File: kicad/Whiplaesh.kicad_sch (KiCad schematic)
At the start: 0 parts

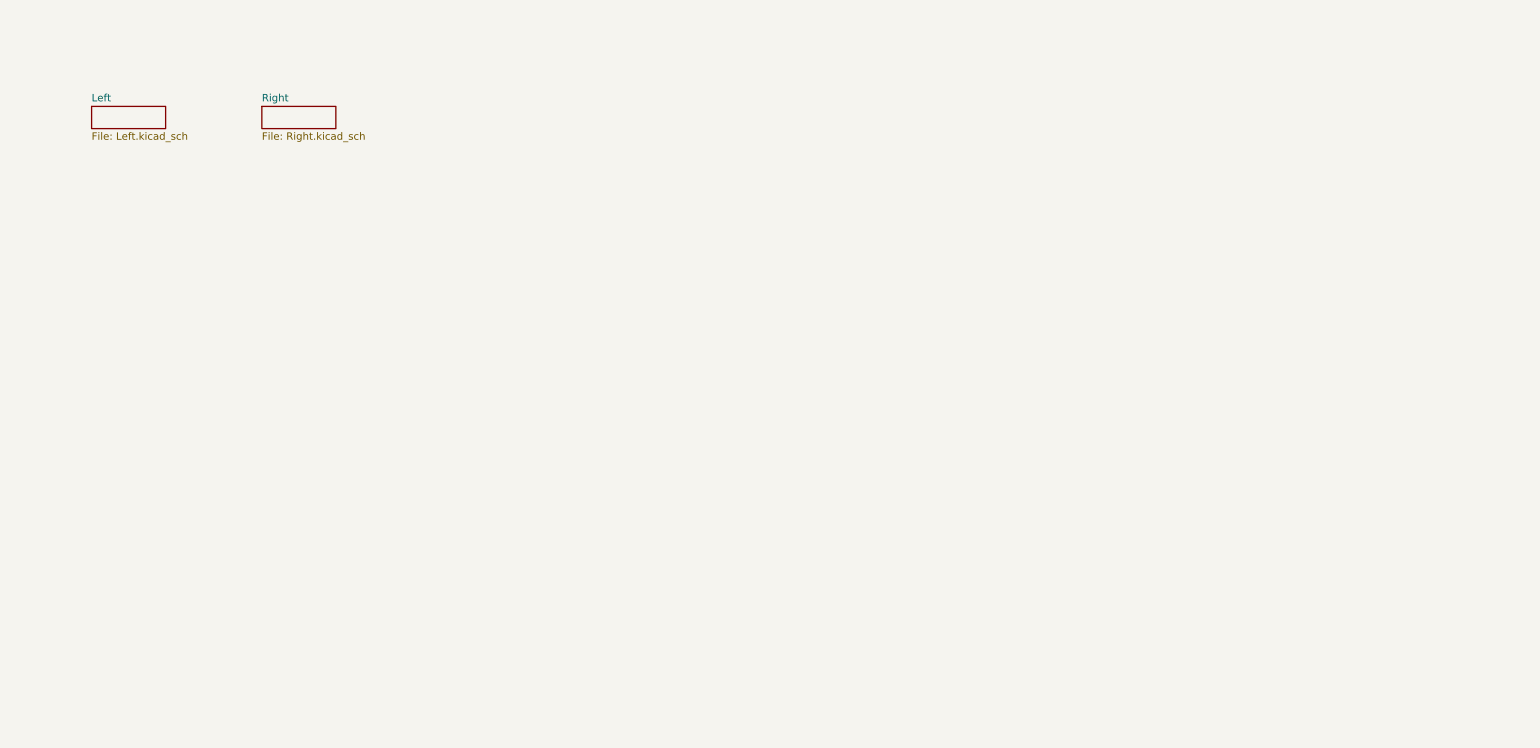
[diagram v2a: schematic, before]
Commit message: add right board in ergogen config
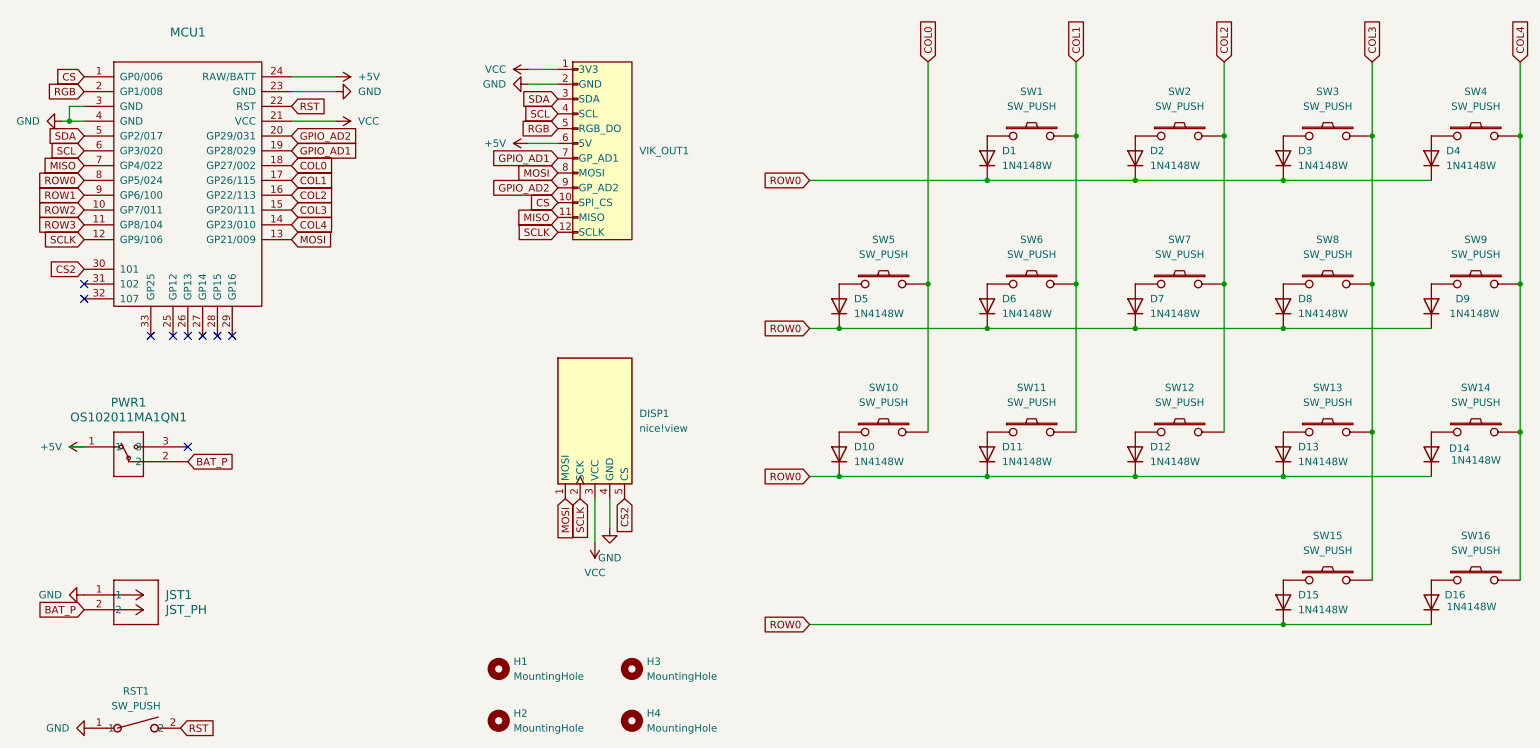
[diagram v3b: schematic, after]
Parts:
- added D1, D10, D11, D12, D13, D14, D15, D16, D2, D3, D4, D5, D6, D7, D8, D9: 1N4148W, fingerpunch:D3_TH_SMD, symbol Diode:1N4148W
- added DISP1: nice!view, fingerpunch:nice_view, symbol nice_view:nice!view
- added H1, H2, H3, H4: MountingHole, MountingHole:MountingHole_2.2mm_M2, symbol Mechanical:MountingHole
- added JST1: JST_PH, Connector_JST:JST_PH_S2B-PH-SM4-TB_1x02-1MP_P2.00mm_Horizontal, symbol CONN_S2B-PH-K-S_JST:S2B-PH-K-SLFSN
- added MCU1: ~, footprints:MCU_nice-nano, symbol RP2040-nrf52840-controller:RP2040-nrf52840-controller
- added PWR1: OS102011MA1QN1, OS102011MA1QN1_CNK, symbol 2024-10-29_23-28-51:OS102011MA1QN1
- added RST1: SW_PUSH, SW_SKHLACA010_ALPS, symbol SW_SKHLACA010_ALPS:SKHLACA010
- added SW1, SW10, SW11, SW12, SW13, SW14, SW15, SW16, SW2, SW3, SW4, SW5, SW6, SW7, SW8, SW9: SW_PUSH, fingerpunch:gateron-ks27-choc-v1-mx-hotswap-reversible, symbol kbd:SW_PUSH
- added VIK_OUT1: ~, fingerpunch:vik-keyboard-connector-horizontal, symbol vik:vik-keyboard-connector
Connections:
- new net: D7.2 (A), SW7.1
- new net: D14.2 (A), SW14.2
- new net: D15.2 (A), SW15.1
- new net: D3.2 (A), SW3.1
- new net: D13.2 (A), SW13.1
- new net: D6.2 (A), SW6.1
- new net: D5.2 (A), SW5.1
- new net: D10.2 (A), SW10.1
- new net: D9.2 (A), SW9.2
- new net: D4.2 (A), SW4.1
- new net: D1.2 (A), SW1.1
- new net: D16.2 (A), SW16.2
- new net: D12.2 (A), SW12.1
- new net: D8.2 (A), SW8.1
- new net: D2.2 (A), SW2.1
- new net: D11.2 (A), SW11.1
- new net +5V: MCU1.24 (RAW/BATT), PWR1.1, VIK_OUT1.6 (5V)
- new net BAT_P: JST1.2, PWR1.2
- new net COL0: MCU1.18 (GP27/002), SW10.2, SW5.2
- new net COL1: MCU1.17 (GP26/115), SW1.2, SW11.2, SW6.2
- new net COL2: MCU1.16 (GP22/113), SW12.2, SW2.2, SW7.2
- new net COL3: MCU1.15 (GP20/111), SW13.2, SW15.2, SW3.2, SW8.2
- new net COL4: MCU1.14 (GP23/010), SW14.1, SW16.1, SW4.2, SW9.1
- new net CS: MCU1.1 (GP0/006), VIK_OUT1.10 (SPI_CS)
- new net CS2: DISP1.5 (CS), MCU1.30 (101)
- new net GND: DISP1.4 (GND), JST1.1, MCU1.23 (GND), MCU1.3 (GND), MCU1.4 (GND), RST1.1, VIK_OUT1.2 (GND)
- new net GPIO_AD1: MCU1.19 (GP28/029), VIK_OUT1.7 (GP_AD1)
- new net GPIO_AD2: MCU1.20 (GP29/031), VIK_OUT1.9 (GP_AD2)
- new net MISO: MCU1.7 (GP4/022), VIK_OUT1.11 (MISO)
- new net MOSI: DISP1.1 (MOSI), MCU1.13 (GP21/009), VIK_OUT1.8 (MOSI)
- new net RGB: MCU1.2 (GP1/008), VIK_OUT1.5 (RGB_DO)
- new net ROW0: D1.1 (K), D10.1 (K), D11.1 (K), D12.1 (K), D13.1 (K), D14.1 (K), D15.1 (K), D16.1 (K), D2.1 (K), D3.1 (K), D4.1 (K), D5.1 (K), D6.1 (K), D7.1 (K), D8.1 (K), D9.1 (K), MCU1.8 (GP5/024)
- new net ROW1: MCU1.9 (GP6/100)
- new net ROW2: MCU1.10 (GP7/011)
- new net ROW3: MCU1.11 (GP8/104)
- new net RST: MCU1.22 (RST), RST1.2
- new net SCL: MCU1.6 (GP3/020), VIK_OUT1.4 (SCL)
- new net SCLK: DISP1.2 (SCK), MCU1.12 (GP9/106), VIK_OUT1.12 (SCLK)
- new net SDA: MCU1.5 (GP2/017), VIK_OUT1.3 (SDA)
- new net VCC: DISP1.3 (VCC), MCU1.21 (VCC), VIK_OUT1.1 (3V3)
- no-connect marks 0 -> 9
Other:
- removed sheet Left
- removed sheet Right
- title: (none) -> Whiplaesh

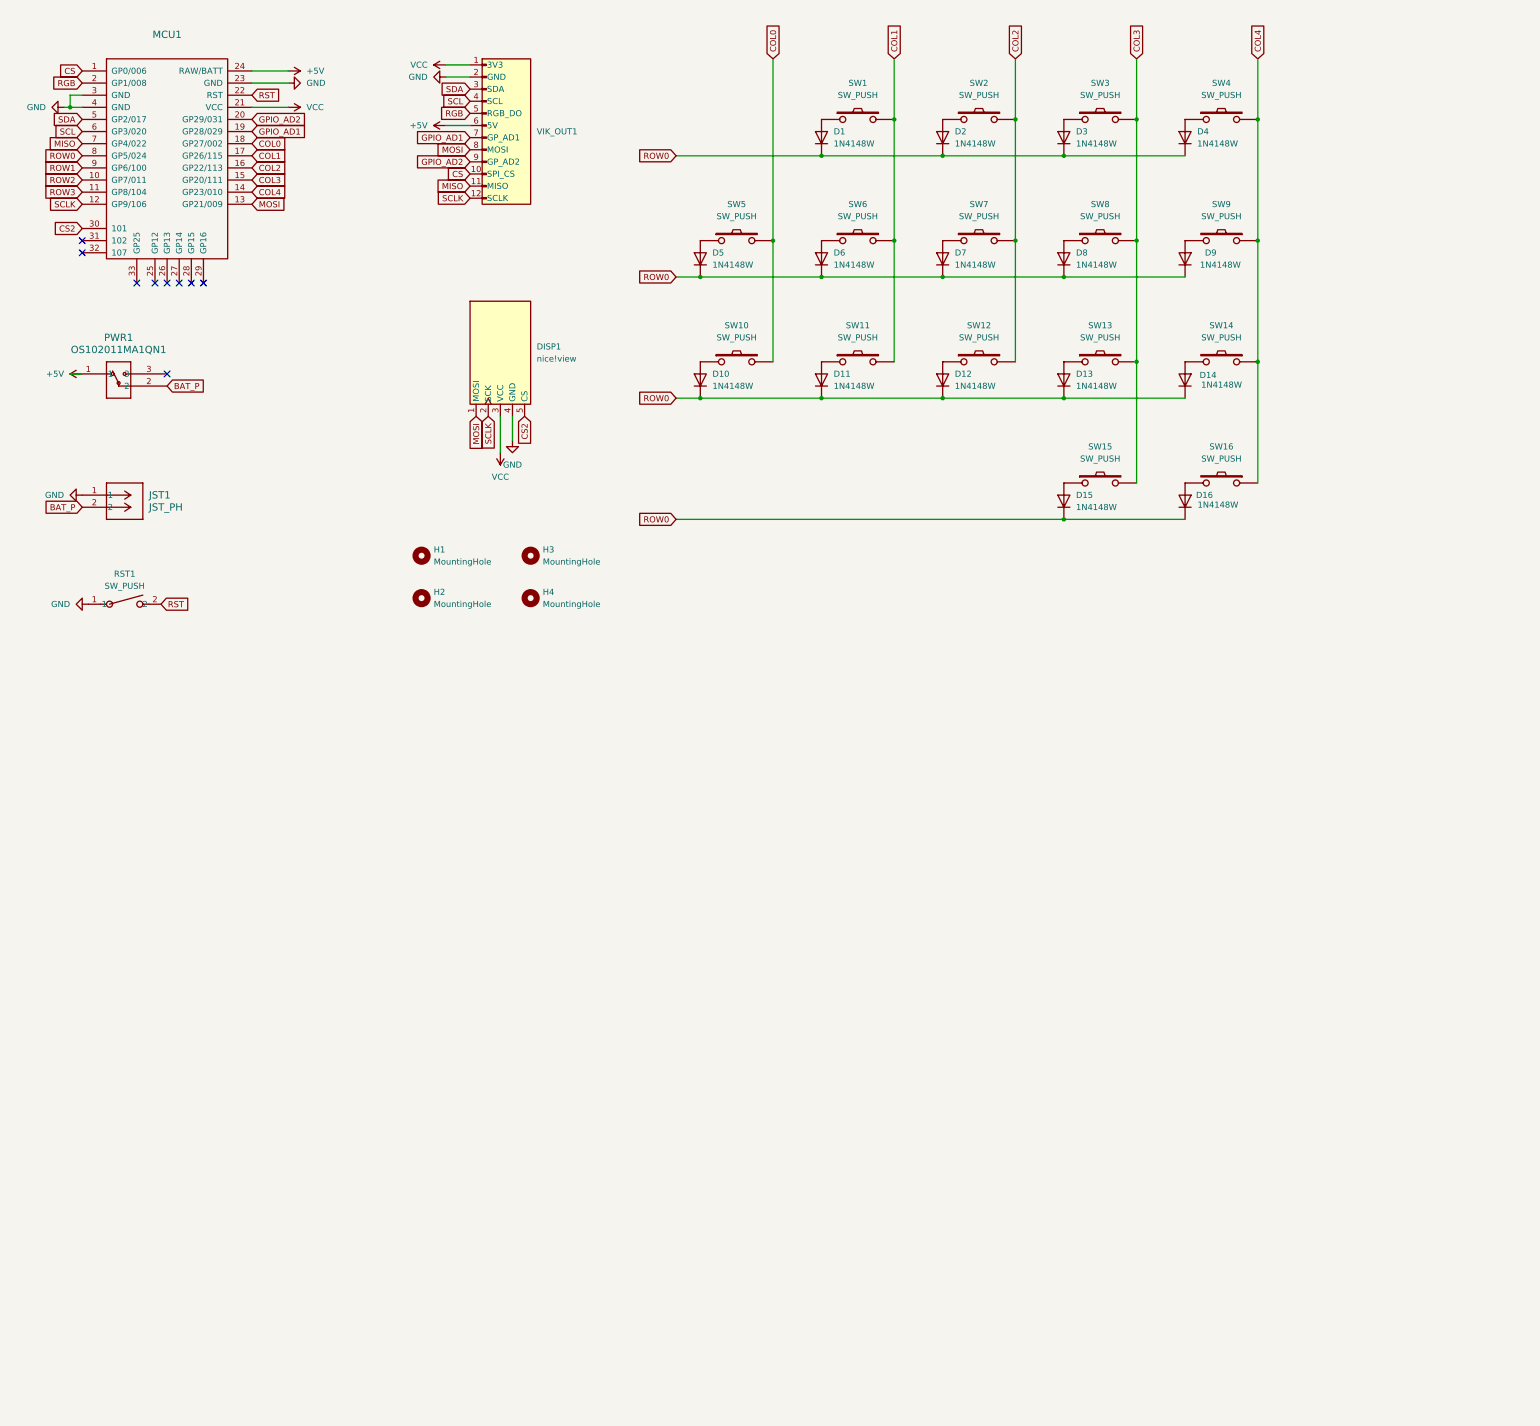
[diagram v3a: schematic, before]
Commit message: Remove nice!view and update schematics and pcb
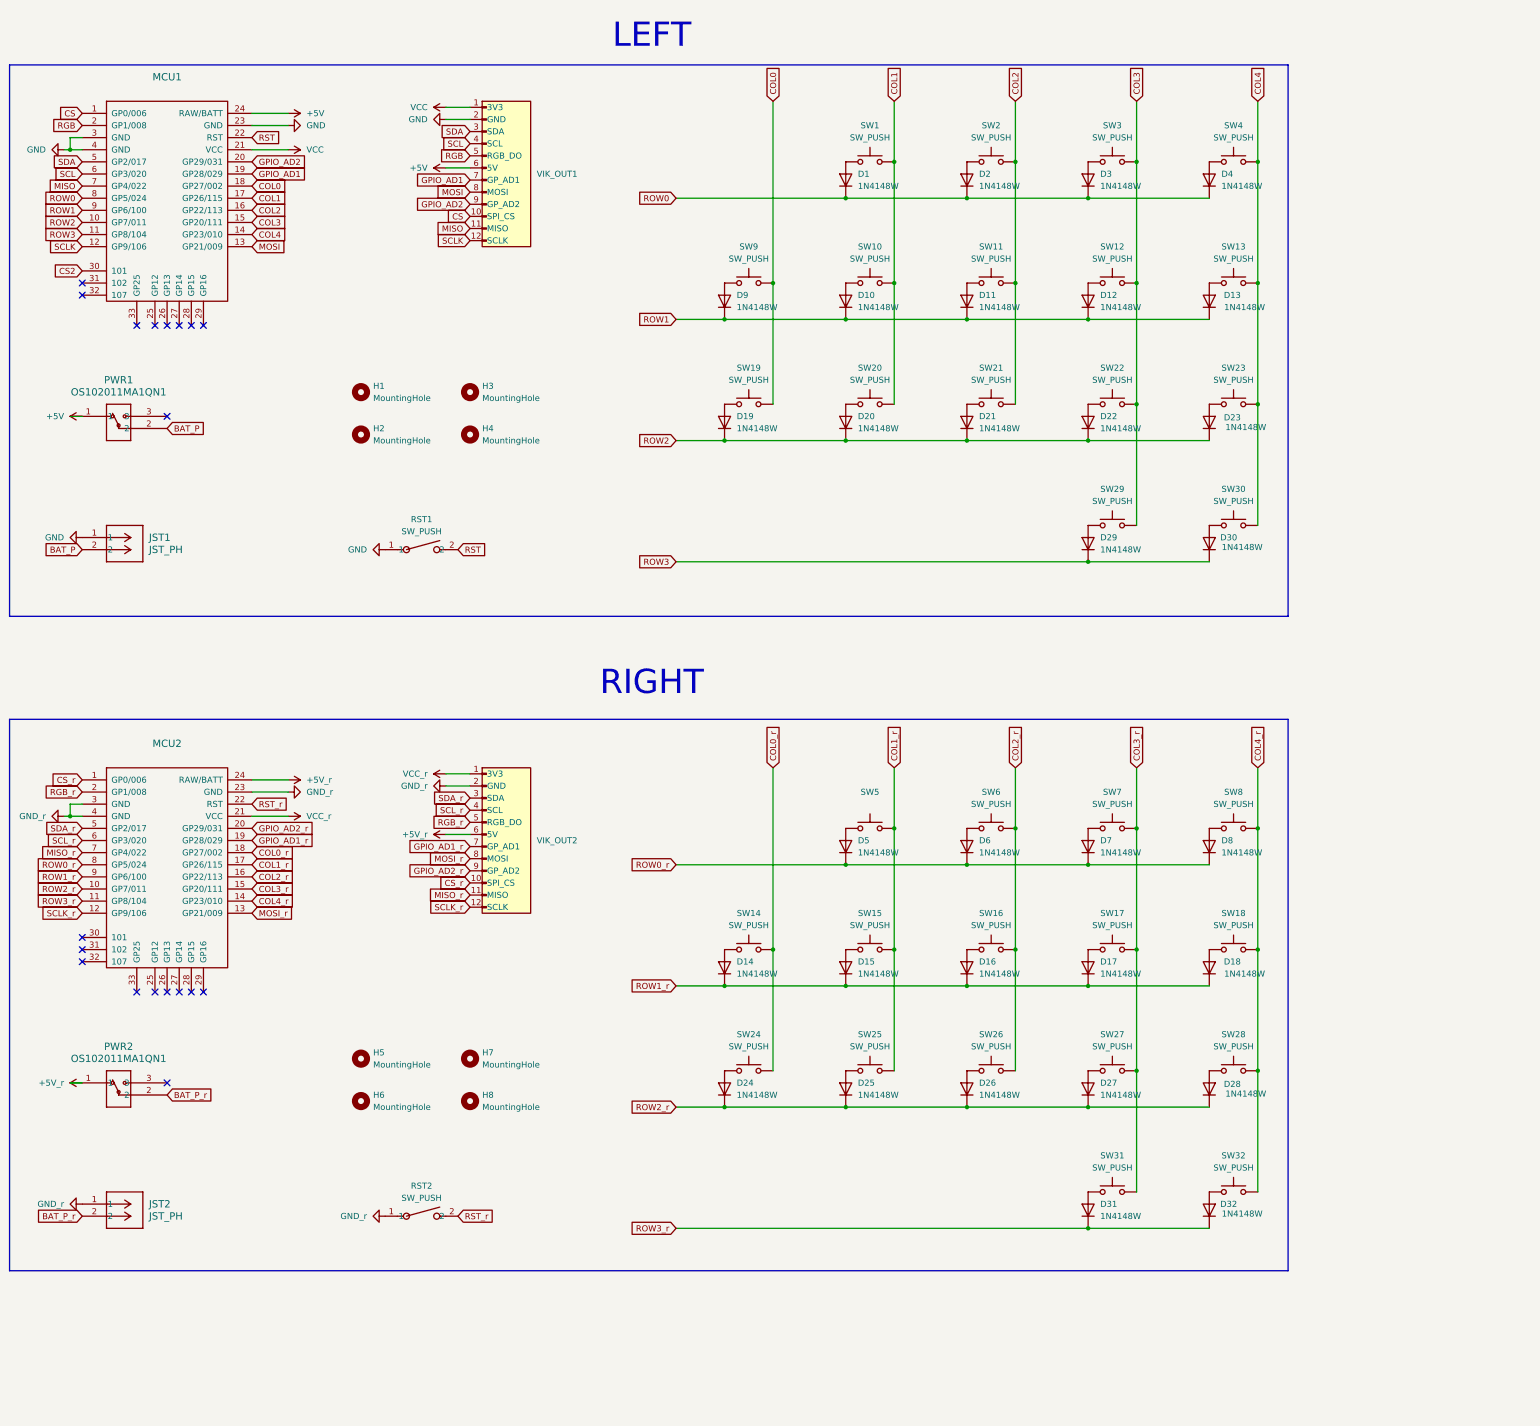
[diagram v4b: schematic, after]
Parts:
- removed DISP1: nice!view, fingerpunch:nice_view, symbol nice_view:nice!view
- added D14, D15, D16, D17, D18, D24, D25, D26, D27, D28, D31, D32, D5, D6, D7, D8: 1N4148W, fingerpunch:D3_TH_SMD, symbol Diode:1N4148W
- added H5, H6, H7, H8: MountingHole, MountingHole:MountingHole_2.2mm_M2, symbol Mechanical:MountingHole
- added JST2: JST_PH, Connector_JST:JST_PH_S2B-PH-K_1x02_P2.00mm_Horizontal, symbol CONN_S2B-PH-K-S_JST:S2B-PH-K-SLFSN
- added MCU2: ~, footprints:MCU_nice-nano, symbol RP2040-nrf52840-controller:RP2040-nrf52840-controller
- added PWR2: OS102011MA1QN1, OS102011MA1QN1_CNK, symbol 2024-10-29_23-28-51:OS102011MA1QN1
- added RST2: SW_PUSH, SW_SKHLACA010_ALPS, symbol SW_SKHLACA010_ALPS:SKHLACA010
- added SW14, SW15, SW16, SW17, SW18, SW24, SW25, SW26, SW27, SW28, SW31, SW32, SW5, SW6, SW7, SW8: SW_PUSH, fingerpunch:gateron-ks27-choc-v1-mx-soldered-and-hotswap, symbol Switch:SW_Push
- added VIK_OUT2: ~, vik:vik-keyboard-connector-horizontal, symbol vik:vik-keyboard-connector
- JST1: footprint Connector_JST:JST_PH_S2B-PH-SM4-TB_1x02-1MP_P2.00mm_Horizontal -> Connector_JST:JST_PH_S2B-PH-K_1x02_P2.00mm_Horizontal
- SW1, SW2, SW3, SW4: footprint fingerpunch:gateron-ks27-choc-v1-mx-hotswap-reversible -> fingerpunch:gateron-ks27-choc-v1-mx-soldered-and-hotswap; symbol kbd:SW_PUSH -> Switch:SW_Push
- SW10: renamed from SW6; footprint fingerpunch:gateron-ks27-choc-v1-mx-hotswap-reversible -> fingerpunch:gateron-ks27-choc-v1-mx-soldered-and-hotswap; symbol kbd:SW_PUSH -> Switch:SW_Push
- SW11: renamed from SW7; footprint fingerpunch:gateron-ks27-choc-v1-mx-hotswap-reversible -> fingerpunch:gateron-ks27-choc-v1-mx-soldered-and-hotswap; symbol kbd:SW_PUSH -> Switch:SW_Push
- SW12: renamed from SW8; footprint fingerpunch:gateron-ks27-choc-v1-mx-hotswap-reversible -> fingerpunch:gateron-ks27-choc-v1-mx-soldered-and-hotswap; symbol kbd:SW_PUSH -> Switch:SW_Push
- SW13: renamed from SW9; footprint fingerpunch:gateron-ks27-choc-v1-mx-hotswap-reversible -> fingerpunch:gateron-ks27-choc-v1-mx-soldered-and-hotswap; symbol kbd:SW_PUSH -> Switch:SW_Push
- SW19: renamed from SW10; footprint fingerpunch:gateron-ks27-choc-v1-mx-hotswap-reversible -> fingerpunch:gateron-ks27-choc-v1-mx-soldered-and-hotswap; symbol kbd:SW_PUSH -> Switch:SW_Push
- SW20: renamed from SW11; footprint fingerpunch:gateron-ks27-choc-v1-mx-hotswap-reversible -> fingerpunch:gateron-ks27-choc-v1-mx-soldered-and-hotswap; symbol kbd:SW_PUSH -> Switch:SW_Push
- SW21: renamed from SW12; footprint fingerpunch:gateron-ks27-choc-v1-mx-hotswap-reversible -> fingerpunch:gateron-ks27-choc-v1-mx-soldered-and-hotswap; symbol kbd:SW_PUSH -> Switch:SW_Push
- SW22: renamed from SW13; footprint fingerpunch:gateron-ks27-choc-v1-mx-hotswap-reversible -> fingerpunch:gateron-ks27-choc-v1-mx-soldered-and-hotswap; symbol kbd:SW_PUSH -> Switch:SW_Push
- SW23: renamed from SW14; footprint fingerpunch:gateron-ks27-choc-v1-mx-hotswap-reversible -> fingerpunch:gateron-ks27-choc-v1-mx-soldered-and-hotswap; symbol kbd:SW_PUSH -> Switch:SW_Push
- SW29: renamed from SW15; footprint fingerpunch:gateron-ks27-choc-v1-mx-hotswap-reversible -> fingerpunch:gateron-ks27-choc-v1-mx-soldered-and-hotswap; symbol kbd:SW_PUSH -> Switch:SW_Push
- SW30: renamed from SW16; footprint fingerpunch:gateron-ks27-choc-v1-mx-hotswap-reversible -> fingerpunch:gateron-ks27-choc-v1-mx-soldered-and-hotswap; symbol kbd:SW_PUSH -> Switch:SW_Push
- SW9: renamed from SW5; footprint fingerpunch:gateron-ks27-choc-v1-mx-hotswap-reversible -> fingerpunch:gateron-ks27-choc-v1-mx-soldered-and-hotswap; symbol kbd:SW_PUSH -> Switch:SW_Push
- VIK_OUT1: footprint fingerpunch:vik-keyboard-connector-horizontal -> vik:vik-keyboard-connector-horizontal
- renumbered D6 to D10, D7 to D11, D8 to D12, D9 to D13, D10 to D19, D11 to D20, D12 to D21, D13 to D22, D14 to D23, D15 to D29, D16 to D30, D5 to D9
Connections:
- net COL4: now also SW13.2, SW23.2, SW30.2; no longer SW13.1, SW23.1, SW30.1
- net ROW0: no longer D10.1 (K), D11.1 (K), D12.1 (K), D13.1 (K), D19.1 (K), D20.1 (K), D21.1 (K), D22.1 (K), D23.1 (K), D29.1 (K), D30.1 (K), D9.1 (K)
- net ROW1: now also D10.1 (K), D11.1 (K), D12.1 (K), D13.1 (K), D9.1 (K)
- net ROW2: now also D19.1 (K), D20.1 (K), D21.1 (K), D22.1 (K), D23.1 (K)
- net ROW3: now also D29.1 (K), D30.1 (K)
- net at D23.2 (A): now also SW23.1; no longer SW23.2
- net at D13.2 (A): now also SW13.1; no longer SW13.2
- net at D30.2 (A): now also SW30.1; no longer SW30.2
- new net: D5.2 (A), SW5.1
- new net: D28.2 (A), SW28.1
- new net: D17.2 (A), SW17.1
- new net: D6.2 (A), SW6.1
- new net: D15.2 (A), SW15.1
- new net: D16.2 (A), SW16.1
- new net: D26.2 (A), SW26.1
- new net: D14.2 (A), SW14.1
- new net: D18.2 (A), SW18.1
- new net: D24.2 (A), SW24.1
- new net: D25.2 (A), SW25.1
- new net: D27.2 (A), SW27.1
- new net: D32.2 (A), SW32.1
- new net: D31.2 (A), SW31.1
- new net: D8.2 (A), SW8.1
- new net: D7.2 (A), SW7.1
- new net +5V_r: MCU2.24 (RAW/BATT), PWR2.1, VIK_OUT2.6 (5V)
- new net BAT_P_r: JST2.2, PWR2.2
- new net COL0_r: MCU2.18 (GP27/002), SW14.2, SW24.2
- new net COL1_r: MCU2.17 (GP26/115), SW15.2, SW25.2, SW5.2
- new net COL2_r: MCU2.16 (GP22/113), SW16.2, SW26.2, SW6.2
- new net COL3_r: MCU2.15 (GP20/111), SW17.2, SW27.2, SW31.2, SW7.2
- new net COL4_r: MCU2.14 (GP23/010), SW18.2, SW28.2, SW32.2, SW8.2
- new net CS_r: MCU2.1 (GP0/006), VIK_OUT2.10 (SPI_CS)
- new net GND_r: JST2.1, MCU2.23 (GND), MCU2.3 (GND), MCU2.4 (GND), RST2.1, VIK_OUT2.2 (GND)
- new net GPIO_AD1_r: MCU2.19 (GP28/029), VIK_OUT2.7 (GP_AD1)
- new net GPIO_AD2_r: MCU2.20 (GP29/031), VIK_OUT2.9 (GP_AD2)
- new net MISO_r: MCU2.7 (GP4/022), VIK_OUT2.11 (MISO)
- new net MOSI_r: MCU2.13 (GP21/009), VIK_OUT2.8 (MOSI)
- new net RGB_r: MCU2.2 (GP1/008), VIK_OUT2.5 (RGB_DO)
- new net ROW0_r: D5.1 (K), D6.1 (K), D7.1 (K), D8.1 (K), MCU2.8 (GP5/024)
- new net ROW1_r: D14.1 (K), D15.1 (K), D16.1 (K), D17.1 (K), D18.1 (K), MCU2.9 (GP6/100)
- new net ROW2_r: D24.1 (K), D25.1 (K), D26.1 (K), D27.1 (K), D28.1 (K), MCU2.10 (GP7/011)
- new net ROW3_r: D31.1 (K), D32.1 (K), MCU2.11 (GP8/104)
- new net RST_r: MCU2.22 (RST), RST2.2
- new net SCLK_r: MCU2.12 (GP9/106), VIK_OUT2.12 (SCLK)
- new net SCL_r: MCU2.6 (GP3/020), VIK_OUT2.4 (SCL)
- new net SDA_r: MCU2.5 (GP2/017), VIK_OUT2.3 (SDA)
- new net VCC_r: MCU2.21 (VCC), VIK_OUT2.1 (3V3)
- no-connect marks 9 -> 19
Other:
- note added: "LEFT"
- note added: "RIGHT"
- moved on the sheet: D1, D10, D11, D12, D13, D19, D2, D20, D21, D22, D23, D29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
